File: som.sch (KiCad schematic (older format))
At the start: 31 parts, among them M1 SC606T

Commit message: Main components placed on board
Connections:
- net CSI0_CLK_N renamed CAM1_DATA_9
- net CSI0_CLK_P renamed CAM1_DATA_8
- net CSI0_LN0_N renamed CAM1_DATA_1
- net CSI0_LN0_P renamed CAM1_DATA_0
- net CSI0_LN1_N renamed CAM1_DATA_3
- net CSI0_LN1_P renamed CAM1_DATA_2
- net CSI0_LN2_N renamed CAM1_DATA_5
- net CSI0_LN2_P renamed CAM1_DATA_4
- net CSI0_LN3_N renamed CAM1_DATA_7
- net CSI0_LN3_P renamed CAM1_DATA_6
- net CSI1_CLK_N renamed CAM2_DATA_9
- net CSI1_CLK_P renamed CAM2_DATA_8
- net CSI1_LN0_N renamed CAM2_DATA_1
- net CSI1_LN0_P renamed CAM2_DATA_0
- net CSI1_LN1_N renamed CAM2_DATA_3
- net CSI1_LN1_P renamed CAM2_DATA_2
- net CSI1_LN2_N renamed CAM2_DATA_5
- net CSI1_LN2_P renamed CAM2_DATA_4
- net CSI1_LN3_N renamed CAM2_DATA_7
- net CSI1_LN3_P renamed CAM2_DATA_6
- net DSI0_CLK_N renamed SoMtoHDMI_DATA_9
- net DSI0_CLK_P renamed SoMtoHDMI_DATA_8
- net DSI0_LN0_N renamed SoMtoHDMI_DATA_1
- net DSI0_LN0_P renamed SoMtoHDMI_DATA_0
- net DSI0_LN1_N renamed SoMtoHDMI_DATA_3
- net DSI0_LN1_P renamed SoMtoHDMI_DATA_2
- net DSI0_LN2_N renamed SoMtoHDMI_DATA_5
- net DSI0_LN2_P renamed SoMtoHDMI_DATA_4
- net DSI0_LN3_N renamed SoMtoHDMI_DATA_7
- net DSI0_LN3_P renamed SoMtoHDMI_DATA_6
- net DSI1_CLK_N renamed SoMtoDisplay_DATA_9
- net DSI1_CLK_P renamed SoMtoDisplay_DATA_8
- net DSI1_LN0_N renamed SoMtoDisplay_DATA_1
- net DSI1_LN0_P renamed SoMtoDisplay_DATA_0
- net DSI1_LN1_N renamed SoMtoDisplay_DATA_3
- net DSI1_LN1_P renamed SoMtoDisplay_DATA_2
- net DSI1_LN2_N renamed SoMtoDisplay_DATA_5
- net DSI1_LN2_P renamed SoMtoDisplay_DATA_4
- net DSI1_LN3_N renamed SoMtoDisplay_DATA_7
- net DSI1_LN3_P renamed SoMtoDisplay_DATA_6
- net SD_CLK renamed SD_DATA_4
- net SD_CMD renamed SD_DATA_5
- net SD_DATA0 renamed SD_DATA_0
- net SD_DATA1 renamed SD_DATA_1
- net SD_DATA2 renamed SD_DATA_2
- net SD_DATA3 renamed SD_DATA_3
- net SD_DET renamed SD_DATA_6
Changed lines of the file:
@@
 	12750 3500 11650 3500
 Text Label 12000 2900 0    50   ~ 0
-CSI0_LN0_N
+CAM1_DATA_1
 Text Label 12000 2800 0    50   ~ 0
-CSI0_LN0_P
+CAM1_DATA_0
 Text Label 12000 3100 0    50   ~ 0
-CSI0_LN1_N
+CAM1_DATA_3
 Text Label 12000 3000 0    50   ~ 0
-CSI0_LN1_P
+CAM1_DATA_2
 Text Label 12000 3300 0    50   ~ 0
-CSI0_LN2_N
+CAM1_DATA_5
 Text Label 12000 3200 0    50   ~ 0
-CSI0_LN2_P
+CAM1_DATA_4
 Text Label 12000 3500 0    50   ~ 0
-CSI0_LN3_N
+CAM1_DATA_7
 Text Label 12000 3400 0    50   ~ 0
-CSI0_LN3_P
+CAM1_DATA_6
 Text Label 12000 2700 0    50   ~ 0
-CSI0_CLK_N
+CAM1_DATA_9
 Text Label 12000 2600 0    50   ~ 0
-CSI0_CLK_P
+CAM1_DATA_8
 Text GLabel 11300 2500 0    50   Input ~ 0
-CAM1_DATA
+CAM1_DATA_[0...9]
 Wire Bus Line
 	11550 2500 11300 2500
@@
 	11550 3700 11650 3800
 Text GLabel 11300 3600 0    50   Input ~ 0
-CAM2_DATA
+CAM2_DATA_[0...9]
 Wire Bus Line
 	11550 3600 11300 3600
@@
 NoConn ~ 5000 6250
 Text Label 1850 4850 0    50   ~ 0
-SD_DET
+SD_DATA_6
 Text Label 1850 4950 0    50   ~ 0
-SD_DATA3
+SD_DATA_3
 Text Label 1850 5050 0    50   ~ 0
-SD_DATA2
+SD_DATA_2
 Text Label 1850 5150 0    50   ~ 0
-SD_DATA1
+SD_DATA_1
 Text Label 1850 5250 0    50   ~ 0
-SD_DATA0
+SD_DATA_0
 Text Label 1850 5350 0    50   ~ 0
-SD_CMD
+SD_DATA_5
 Text Label 1850 5450 0    50   ~ 0
-SD_CLK
+SD_DATA_4
 Wire Wire Line
 	1850 4850 2800 4850
@@
 	1750 4650 1600 4650
 Text GLabel 1600 4650 0    50   Input ~ 0
-SD_DATA
+SD_DATA_[0...6]
 Text GLabel 1600 4500 0    50   Input ~ 0
 SD_LDO11
@@
 NoConn ~ 5000 5750
 NoConn ~ 5000 5850
-Text Label 15050 3500 2    50   ~ 0
-DSI1_LN3_N
-Text Label 15050 3400 2    50   ~ 0
-DSI1_LN3_P
-Text Label 15050 3300 2    50   ~ 0
-DSI1_LN2_N
-Text Label 15050 3200 2    50   ~ 0
-DSI1_LN2_P
-Text Label 15050 2700 2    50   ~ 0
-DSI1_CLK_N
-Text Label 15050 2600 2    50   ~ 0
-DSI1_CLK_P
-Text Label 15050 3100 2    50   ~ 0
-DSI1_LN1_N
-Text Label 15050 3000 2    50   ~ 0
-DSI1_LN1_P
-Text Label 15050 2900 2    50   ~ 0
-DSI1_LN0_N
-Text Label 15050 2800 2    50   ~ 0
-DSI1_LN0_P
-Wire Wire Line
-	14550 3500 15050 3500
-Wire Wire Line
-	15050 3400 14550 3400
-Wire Wire Line
-	14550 3300 15050 3300
-Wire Wire Line
-	15050 3200 14550 3200
-Wire Wire Line
-	14550 2700 15050 2700
-Wire Wire Line
-	15050 2600 14550 2600
-Wire Wire Line
-	14550 3100 15050 3100
-Wire Wire Line
-	15050 3000 14550 3000
-Wire Wire Line
-	14550 2900 15050 2900
-Wire Wire Line
-	15050 2800 14550 2800
-Entry Wire Line
-	15150 3600 15050 3500
-Entry Wire Line
-	15150 3500 15050 3400
-Entry Wire Line
-	15150 3400 15050 3300
-Entry Wire Line
-	15150 3300 15050 3200
-Entry Wire Line
-	15150 3200 15050 3100
-Entry Wire Line
-	15150 3100 15050 3000
-Entry Wire Line
-	15150 3000 15050 2900
-Entry Wire Line
-	15150 2900 15050 2800
-Entry Wire Line
-	15150 2900 15050 2800
-Entry Wire Line
-	15150 2800 15050 2700
-Entry Wire Line
-	15150 2700 15050 2600
-Wire Bus Line
-	15150 3600 15200 3600
-Text GLabel 15200 3600 2    50   Input ~ 0
-SoMtoHDMI_DATA
-Text Label 15050 2400 2    50   ~ 0
-DSI0_LN3_N
-Text Label 15050 2300 2    50   ~ 0
-DSI0_LN3_P
-Text Label 15050 2200 2    50   ~ 0
-DSI0_LN2_N
-Text Label 15050 2100 2    50   ~ 0
-DSI0_LN2_P
-Text Label 15050 1600 2    50   ~ 0
-DSI0_CLK_N
-Text Label 15050 1500 2    50   ~ 0
-DSI0_CLK_P
-Text Label 15050 2000 2    50   ~ 0
-DSI0_LN1_N
-Text Label 15050 1900 2    50   ~ 0
-DSI0_LN1_P
-Text Label 15050 1800 2    50   ~ 0
-DSI0_LN0_N
-Text Label 15050 1700 2    50   ~ 0
-DSI0_LN0_P
-Wire Wire Line
-	14550 2400 15050 2400
-Wire Wire Line
-	15050 2300 14550 2300
-Wire Wire Line
-	14550 2200 15050 2200
-Wire Wire Line
-	15050 2100 14550 2100
-Wire Wire Line
-	14550 1600 15050 1600
-Wire Wire Line
-	15050 1500 14550 1500
-Wire Wire Line
-	14550 2000 15050 2000
-Wire Wire Line
-	15050 1900 14550 1900
-Wire Wire Line
-	14550 1800 15050 1800
-Wire Wire Line
-	15050 1700 14550 1700
-Entry Wire Line
-	15150 2500 15050 2400
-Entry Wire Line
-	15150 2400 15050 2300
-Entry Wire Line
-	15150 2300 15050 2200
-Entry Wire Line
-	15150 2200 15050 2100
-Entry Wire Line
-	15150 2100 15050 2000
-Entry Wire Line
-	15150 2000 15050 1900
-Entry Wire Line
-	15150 1900 15050 1800
-Entry Wire Line
-	15150 1800 15050 1700
-Entry Wire Line
-	15150 1800 15050 1700
-Entry Wire Line
-	15150 1700 15050 1600
-Entry Wire Line
-	15150 1600 15050 1500
-Wire Bus Line
-	15150 2500 15200 2500
-Text GLabel 15200 2500 2    50   Input ~ 0
-SoMtoDisplay_DATA
+Text Label 15400 3500 2    50   ~ 0
+SoMtoDisplay_DATA_7
+Text Label 15400 3400 2    50   ~ 0
+SoMtoDisplay_DATA_6
+Text Label 15400 3300 2    50   ~ 0
+SoMtoDisplay_DATA_5
+Text Label 15400 3200 2    50   ~ 0
+SoMtoDisplay_DATA_4
+Text Label 15400 2700 2    50   ~ 0
+SoMtoDisplay_DATA_9
+Text Label 15400 2600 2    50   ~ 0
+SoMtoDisplay_DATA_8
+Text Label 15400 3100 2    50   ~ 0
+SoMtoDisplay_DATA_3
+Text Label 15400 3000 2    50   ~ 0
+SoMtoDisplay_DATA_2
+Text Label 15400 2900 2    50   ~ 0
+SoMtoDisplay_DATA_1
+Text Label 15400 2800 2    50   ~ 0
+SoMtoDisplay_DATA_0
+Wire Wire Line
+	14550 3500 15400 3500
+Wire Wire Line
+	15400 3400 14550 3400
+Wire Wire Line
+	14550 3300 15400 3300
+Wire Wire Line
+	15400 3200 14550 3200
+Wire Wire Line
+	14550 2700 15400 2700
+Wire Wire Line
+	15400 2600 14550 2600
+Wire Wire Line
+	14550 3100 15400 3100
+Wire Wire Line
+	15400 3000 14550 3000
+Wire Wire Line
+	14550 2900 15400 2900
+Wire Wire Line
+	15400 2800 14550 2800
+Entry Wire Line
+	15500 3600 15400 3500
+Entry Wire Line
+	15500 3500 15400 3400
+Entry Wire Line
+	15500 3400 15400 3300
+Entry Wire Line
+	15500 3300 15400 3200
+Entry Wire Line
+	15500 3200 15400 3100
+Entry Wire Line
+	15500 3100 15400 3000
+Entry Wire Line
+	15500 3000 15400 2900
+Entry Wire Line
+	15500 2900 15400 2800
+Entry Wire Line
+	15500 2900 15400 2800
+Entry Wire Line
+	15500 2800 15400 2700
+Entry Wire Line
+	15500 2700 15400 2600
+Text GLabel 15500 1600 2    50   Input ~ 0
+SoMtoHDMI_DATA_[0...9]
+Text Label 15400 2400 2    50   ~ 0
+SoMtoHDMI_DATA_7
+Text Label 15400 2300 2    50   ~ 0
+SoMtoHDMI_DATA_6
+Text Label 15400 2200 2    50   ~ 0
+SoMtoHDMI_DATA_5
+Text Label 15400 2100 2    50   ~ 0
+SoMtoHDMI_DATA_4
+Text Label 15400 1500 2    50   ~ 0
+SoMtoHDMI_DATA_8
+Text Label 15400 2000 2    50   ~ 0
+SoMtoHDMI_DATA_3
+Text Label 15400 1900 2    50   ~ 0
+SoMtoHDMI_DATA_2
+Text Label 15400 1800 2    50   ~ 0
+SoMtoHDMI_DATA_1
+Text Label 15400 1700 2    50   ~ 0
+SoMtoHDMI_DATA_0
+Wire Wire Line
+	14550 2400 15400 2400
+Wire Wire Line
+	15400 2300 14550 2300
+Wire Wire Line
+	14550 2200 15400 2200
+Wire Wire Line
+	15400 2100 14550 2100
+Wire Wire Line
+	14550 1600 15400 1600
+Wire Wire Line
+	15400 1500 14550 1500
+Wire Wire Line
+	14550 2000 15400 2000
+Wire Wire Line
+	15400 1900 14550 1900
+Wire Wire Line
+	14550 1800 15400 1800
+Wire Wire Line
+	15400 1700 14550 1700
+Entry Wire Line
+	15500 2500 15400 2400
+Entry Wire Line
+	15500 2400 15400 2300
+Entry Wire Line
+	15500 2300 15400 2200
+Entry Wire Line
+	15500 2200 15400 2100
+Entry Wire Line
+	15500 2100 15400 2000
+Entry Wire Line
+	15500 2000 15400 1900
+Entry Wire Line
+	15500 1900 15400 1800
+Entry Wire Line
+	15500 1800 15400 1700
+Entry Wire Line
+	15500 1800 15400 1700
+Entry Wire Line
+	15500 1700 15400 1600
+Entry Wire Line
+	15500 1600 15400 1500
+Text GLabel 15500 3600 2    50   Input ~ 0
+SoMtoDisplay_DATA_[0...9]
 Text GLabel 7400 2600 0    50   Input ~ 0
 HDMI_I2C_SCL
@@
 HDMI_I2C_SDA
 Text Label 12000 4000 0    50   ~ 0
-CSI1_LN0_N
+CAM2_DATA_1
 Text Label 12000 3900 0    50   ~ 0
-CSI1_LN0_P
+CAM2_DATA_0
 Text Label 12000 4200 0    50   ~ 0
-CSI1_LN1_N
+CAM2_DATA_3
 Text Label 12000 4100 0    50   ~ 0
-CSI1_LN1_P
+CAM2_DATA_2
 Text Label 12000 4400 0    50   ~ 0
-CSI1_LN2_N
+CAM2_DATA_5
 Text Label 12000 4300 0    50   ~ 0
-CSI1_LN2_P
+CAM2_DATA_4
 Text Label 12000 4600 0    50   ~ 0
-CSI1_LN3_N
+CAM2_DATA_7
 Text Label 12000 4500 0    50   ~ 0
-CSI1_LN3_P
+CAM2_DATA_6
 Text Label 12000 3800 0    50   ~ 0
-CSI1_CLK_N
+CAM2_DATA_9
 Text Label 12000 3700 0    50   ~ 0
-CSI1_CLK_P
+CAM2_DATA_8
 Wire Wire Line
 	11650 3900 12750 3900
@@
 Text GLabel 5000 2250 2    50   Input ~ 0
 ANT-WIFI
+Text Label 15400 1600 2    50   ~ 0
+SoMtoHDMI_DATA_9
 Wire Bus Line
 	1750 4650 1750 5350
@@
 	11550 2500 11550 3400
 Wire Bus Line
-	15150 2700 15150 3600
-Wire Bus Line
-	15150 1600 15150 2500
+	15500 2700 15500 3600
+Wire Bus Line
+	15500 1600 15500 2500
 $EndSCHEMATC

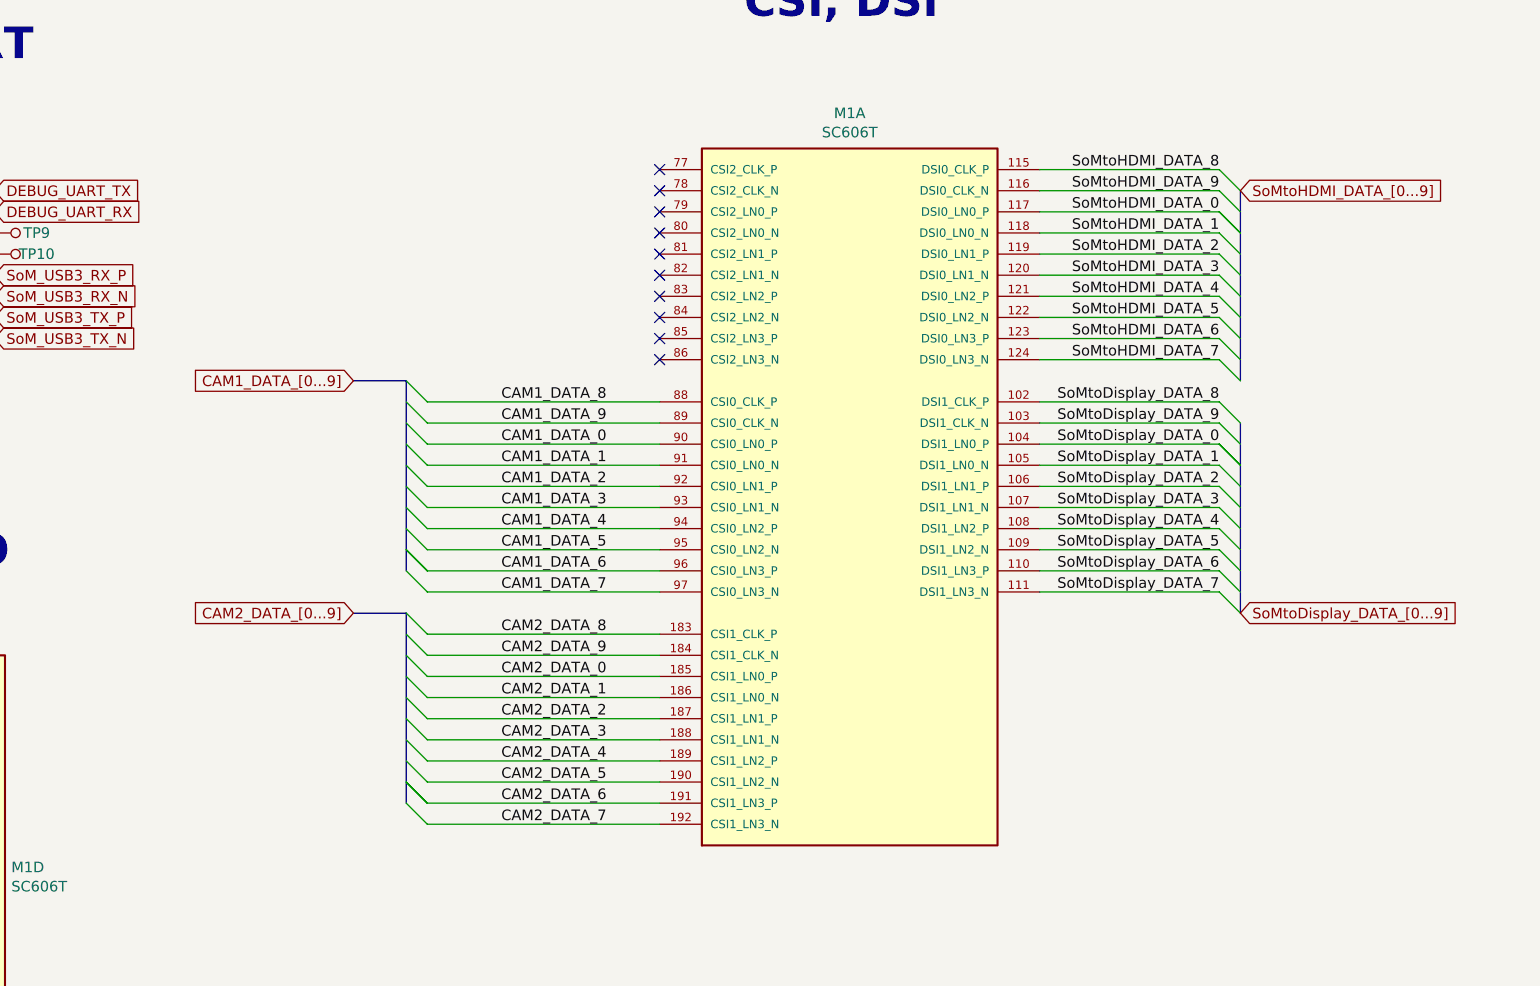
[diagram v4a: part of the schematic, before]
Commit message: FFC and general display camera connectors distributed on board
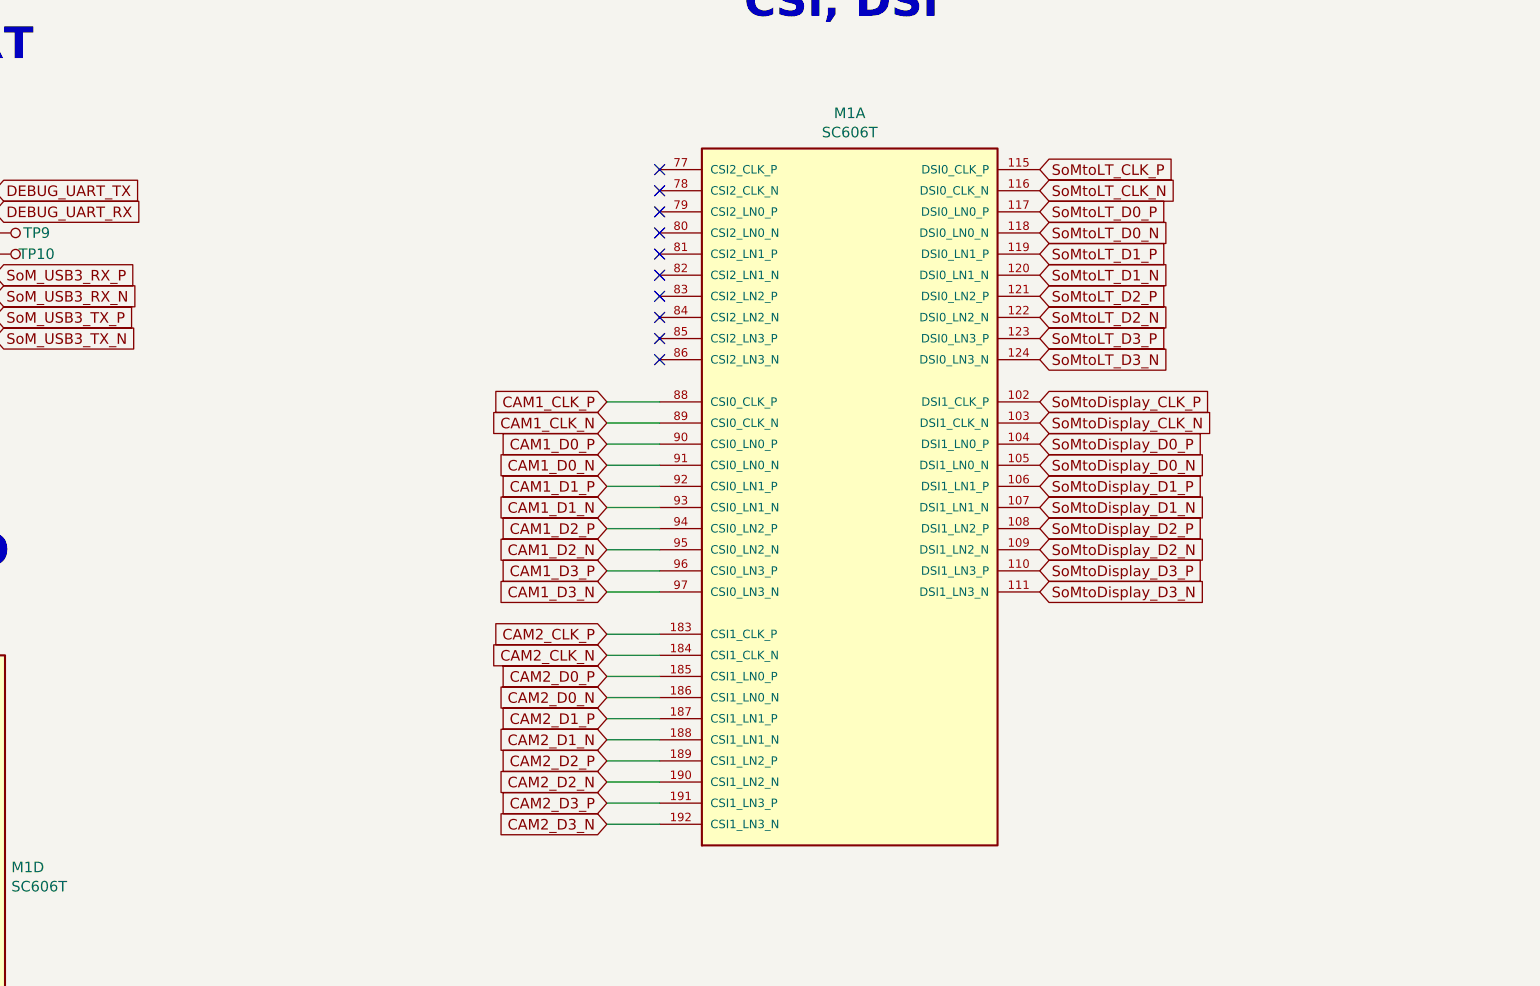
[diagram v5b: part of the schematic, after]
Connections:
- net CAM1_DATA_0 renamed CAM1_D0_P
- net CAM1_DATA_1 renamed CAM1_D0_N
- net CAM1_DATA_2 renamed CAM1_D1_P
- net CAM1_DATA_3 renamed CAM1_D1_N
- net CAM1_DATA_4 renamed CAM1_D2_P
- net CAM1_DATA_5 renamed CAM1_D2_N
- net CAM1_DATA_6 renamed CAM1_D3_P
- net CAM1_DATA_7 renamed CAM1_D3_N
- net CAM1_DATA_8 renamed CAM1_CLK_P
- net CAM1_DATA_9 renamed CAM1_CLK_N
- net CAM2_DATA_0 renamed CAM2_D0_P
- net CAM2_DATA_1 renamed CAM2_D0_N
- net CAM2_DATA_2 renamed CAM2_D1_P
- net CAM2_DATA_3 renamed CAM2_D1_N
- net CAM2_DATA_4 renamed CAM2_D2_P
- net CAM2_DATA_5 renamed CAM2_D2_N
- net CAM2_DATA_6 renamed CAM2_D3_P
- net CAM2_DATA_7 renamed CAM2_D3_N
- net CAM2_DATA_8 renamed CAM2_CLK_P
- net CAM2_DATA_9 renamed CAM2_CLK_N
- net SoMtoDisplay_DATA_0 renamed SoMtoDisplay_D0_P
- net SoMtoDisplay_DATA_1 renamed SoMtoDisplay_D0_N
- net SoMtoDisplay_DATA_2 renamed SoMtoDisplay_D1_P
- net SoMtoDisplay_DATA_3 renamed SoMtoDisplay_D1_N
- net SoMtoDisplay_DATA_4 renamed SoMtoDisplay_D2_P
- net SoMtoDisplay_DATA_5 renamed SoMtoDisplay_D2_N
- net SoMtoDisplay_DATA_6 renamed SoMtoDisplay_D3_P
- net SoMtoDisplay_DATA_7 renamed SoMtoDisplay_D3_N
- net SoMtoDisplay_DATA_8 renamed SoMtoDisplay_CLK_P
- net SoMtoDisplay_DATA_9 renamed SoMtoDisplay_CLK_N
- net SoMtoHDMI_DATA_0 renamed SoMtoLT_D0_P
- net SoMtoHDMI_DATA_1 renamed SoMtoLT_D0_N
- net SoMtoHDMI_DATA_2 renamed SoMtoLT_D1_P
- net SoMtoHDMI_DATA_3 renamed SoMtoLT_D1_N
- net SoMtoHDMI_DATA_4 renamed SoMtoLT_D2_P
- net SoMtoHDMI_DATA_5 renamed SoMtoLT_D2_N
- net SoMtoHDMI_DATA_6 renamed SoMtoLT_D3_P
- net SoMtoHDMI_DATA_7 renamed SoMtoLT_D3_N
- net SoMtoHDMI_DATA_8 renamed SoMtoLT_CLK_P
- net SoMtoHDMI_DATA_9 renamed SoMtoLT_CLK_N
